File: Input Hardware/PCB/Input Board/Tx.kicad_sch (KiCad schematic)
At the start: 40 parts

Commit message: WEEEE
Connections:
- net GNDPWR is gone; now on net GND: U?.1 (PGND), U?.1 (PGND), U?.1 (PGND), U?.1 (PGND), U?.10 (PGND), U?.10 (PGND), U?.10 (PGND), U?.10 (PGND), U?.11 (PGND), U?.11 (PGND), U?.11 (PGND), U?.11 (PGND), U?.19 (LGND), U?.19 (LGND), U?.19 (LGND), U?.19 (LGND), U?.20 (PGND), U?.20 (PGND), U?.20 (PGND), U?.20 (PGND)

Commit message: input encoder and LEDs
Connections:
- net ~{SRCLR} is gone; now on net +5V: U?.8 (~{SRCLR}), U?.8 (~{SRCLR}), U?.8 (~{SRCLR}), U?.8 (~{SRCLR})

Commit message: Fix files idc
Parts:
- gave numbers to parts that had none: 40

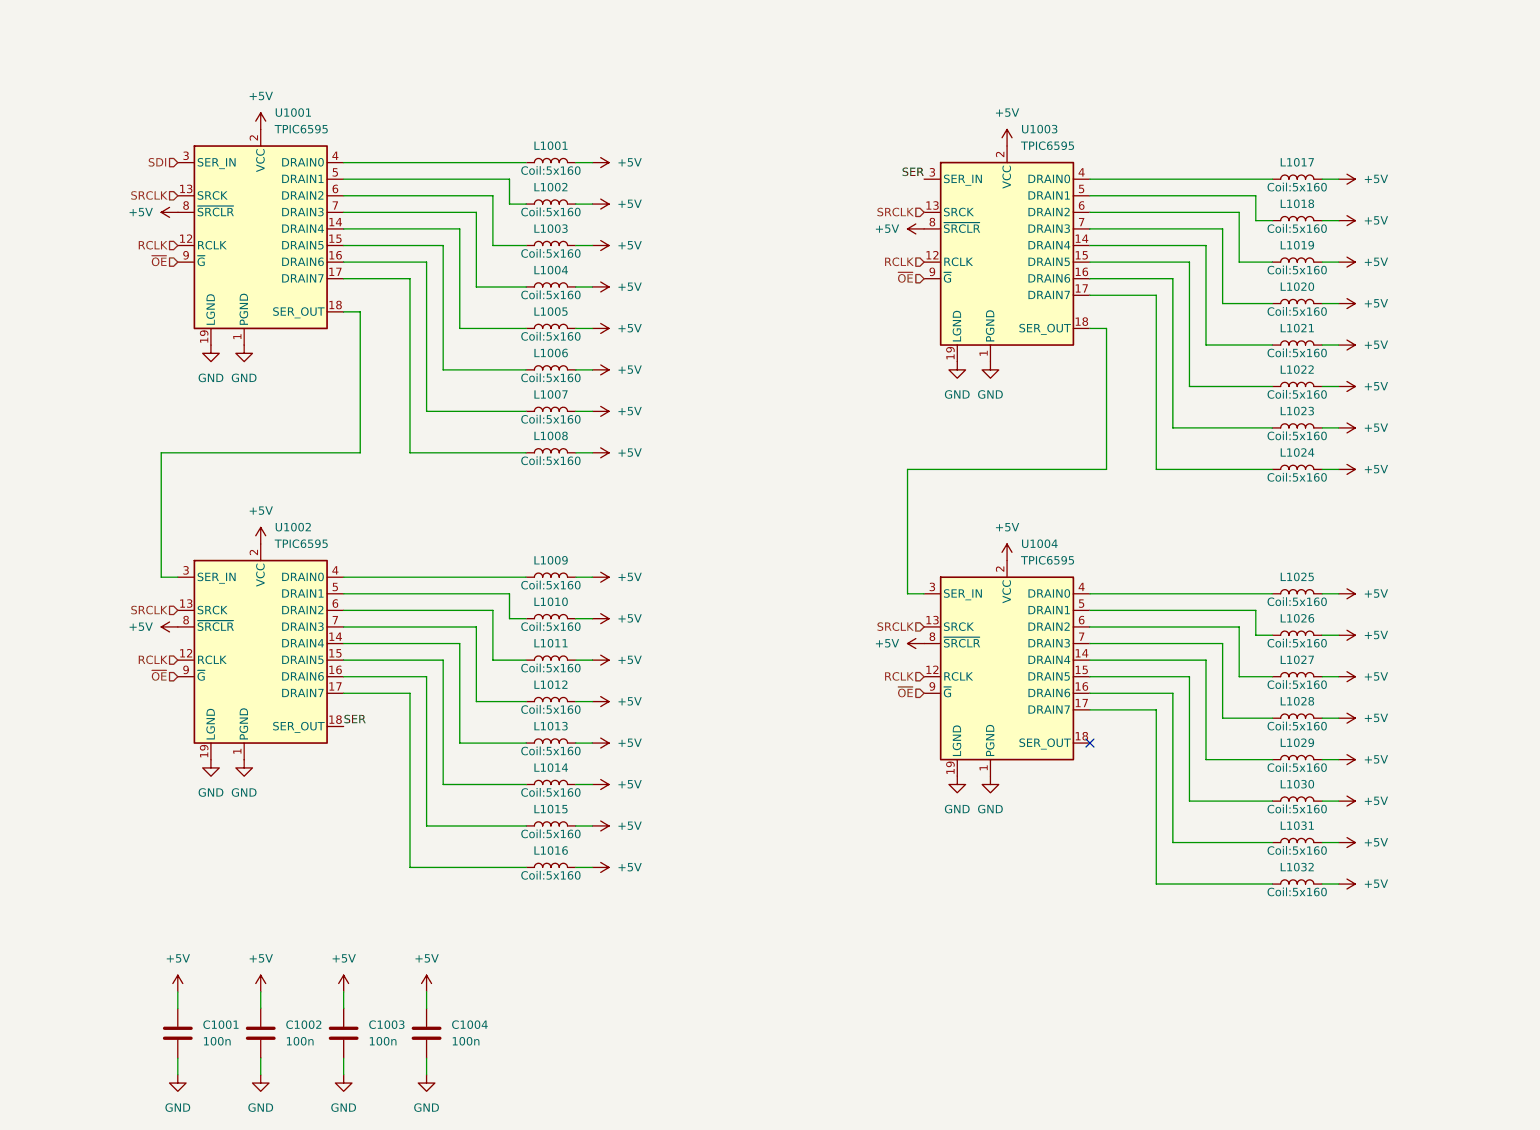
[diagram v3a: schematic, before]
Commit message: driver and root page updates
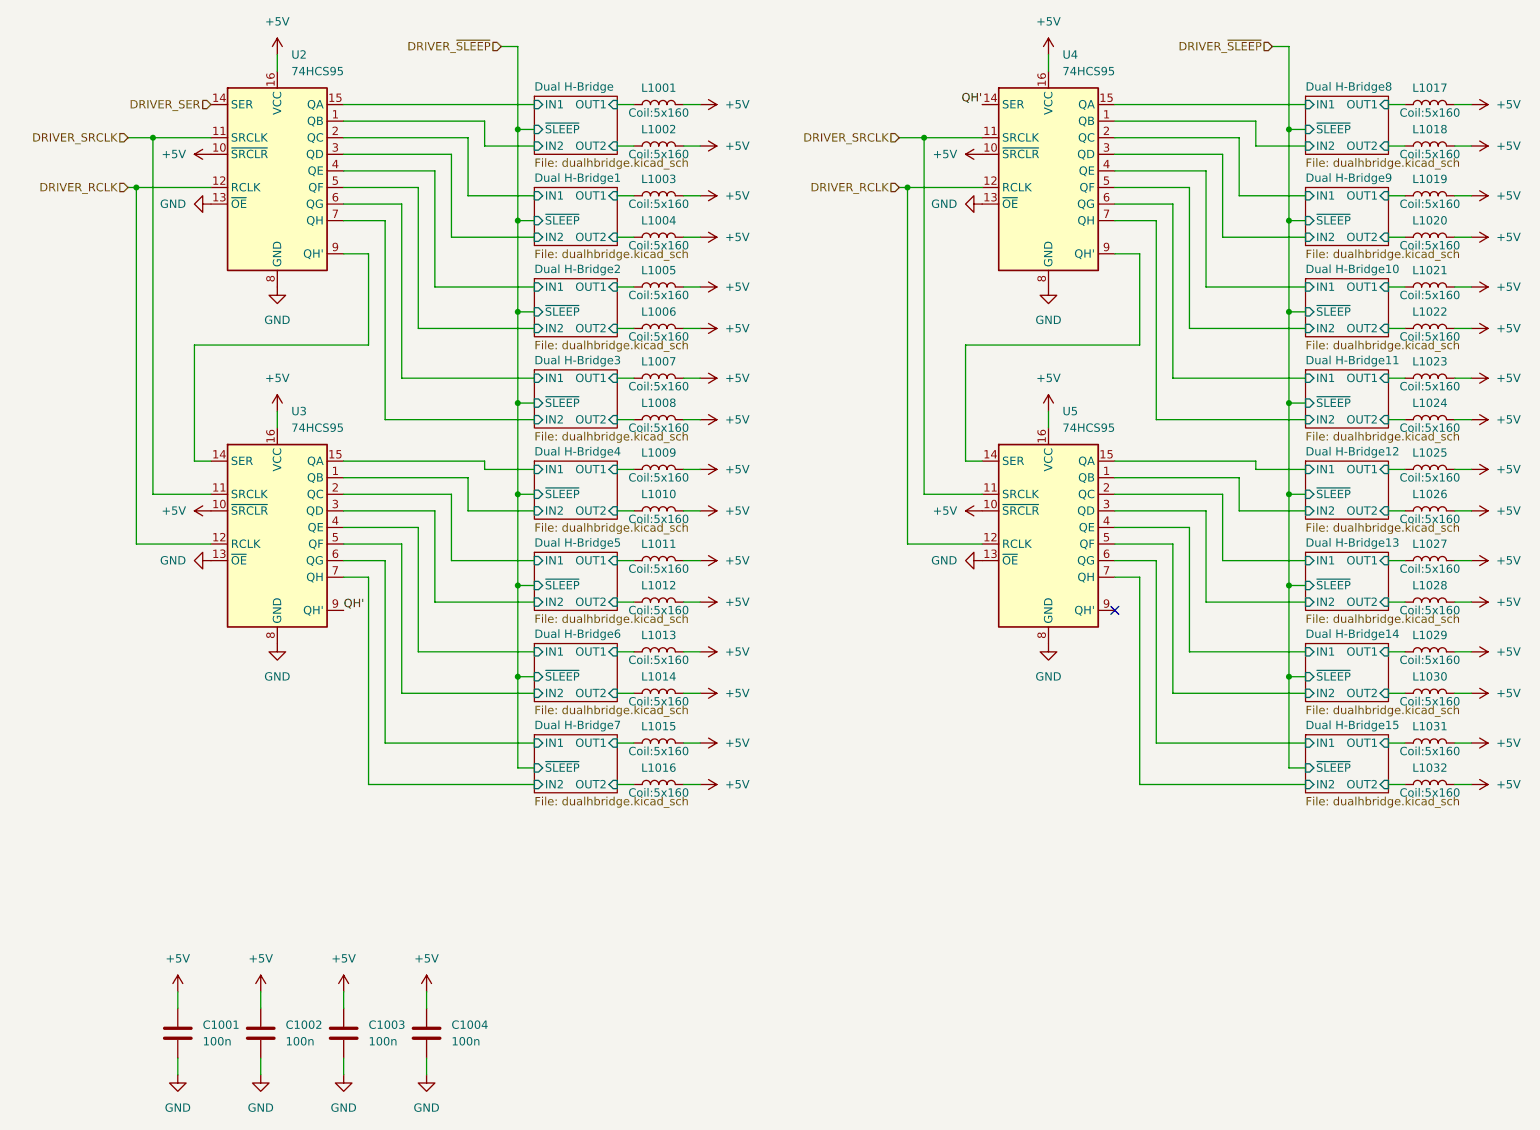
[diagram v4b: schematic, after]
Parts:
- removed U1001, U1002, U1003, U1004: TPIC6595, Package_SO:SOIC-20W_7.5x12.8mm_P1.27mm, symbol Interface_Expansion:TPIC6595
- added U2, U3, U4, U5: 74HCS95, Package_SO:SOIC-16_3.9x9.9mm_P1.27mm, symbol 74xx:74HC595
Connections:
- net +5V: now also U2.10 (~{SRCLR}), U2.16 (VCC), U3.10 (~{SRCLR}), U3.16 (VCC), U4.10 (~{SRCLR}), U4.16 (VCC), U5.10 (~{SRCLR}), U5.16 (VCC)
- net GND: now also U2.13 (~{OE}), U2.8 (GND), U3.13 (~{OE}), U3.8 (GND), U4.13 (~{OE}), U4.8 (GND), U5.13 (~{OE}), U5.8 (GND)
- net Dual H-Bridge9/OUT1: now reaches L1019.1
- net Dual H-Bridge11/OUT2: now reaches L1024.1
- net Dual H-Bridge2/OUT2: now reaches L1006.1
- net Dual H-Bridge1/OUT1: now reaches L1003.1
- net Dual H-Bridge3/OUT2: now reaches L1008.1
- net Dual H-Bridge13/OUT1: now reaches L1027.1
- net Dual H-Bridge3/OUT1: now reaches L1007.1
- net Dual H-Bridge14/OUT2: now reaches L1030.1
- net Dual H-Bridge12/OUT2: now reaches L1026.1
- net Dual H-Bridge1/OUT2: now reaches L1004.1
- net Dual H-Bridge6/OUT1: now reaches L1013.1
- net Dual H-Bridge6/OUT2: now reaches L1014.1
- net Dual H-Bridge5/OUT1: now reaches L1011.1
- net Dual H-Bridge8/OUT1: now reaches L1017.1
- net Dual H-Bridge4/OUT2: now reaches L1010.1
- net Dual H-Bridge15/OUT1: now reaches L1031.1
- net Dual H-Bridge/OUT2: now reaches L1002.1
- net Dual H-Bridge10/OUT1: now reaches L1021.1
- net Dual H-Bridge10/OUT2: now reaches L1022.1
- net Dual H-Bridge11/OUT1: now reaches L1023.1
- net Dual H-Bridge8/OUT2: now reaches L1018.1
- net Dual H-Bridge9/OUT2: now reaches L1020.1
- net Dual H-Bridge/OUT1: now reaches L1001.1
- net Dual H-Bridge2/OUT1: now reaches L1005.1
- net Dual H-Bridge7/OUT1: now reaches L1015.1
- net Dual H-Bridge7/OUT2: now reaches L1016.1
- net Dual H-Bridge4/OUT1: now reaches L1009.1
- net Dual H-Bridge5/OUT2: now reaches L1012.1
- net Dual H-Bridge14/OUT1: now reaches L1029.1
- net Dual H-Bridge15/OUT2: now reaches L1032.1
- net Dual H-Bridge12/OUT1: now reaches L1025.1
- net Dual H-Bridge13/OUT2: now reaches L1028.1
- new net: U2.9 (QH'), U3.14 (SER)
- new net: U4.9 (QH'), U5.14 (SER)
- new net DRIVER_RCLK: U2.12 (RCLK), U3.12 (RCLK), U4.12 (RCLK), U5.12 (RCLK)
- new net DRIVER_SER: U2.14 (SER)
- new net DRIVER_SRCLK: U2.11 (SRCLK), U3.11 (SRCLK), U4.11 (SRCLK), U5.11 (SRCLK)
- new net Dual H-Bridge/IN1: U2.15 (QA)
- new net Dual H-Bridge/IN2: U2.1 (QB)
- new net Dual H-Bridge1/IN1: U2.2 (QC)
- new net Dual H-Bridge1/IN2: U2.3 (QD)
- new net Dual H-Bridge10/IN1: U4.4 (QE)
- new net Dual H-Bridge10/IN2: U4.5 (QF)
- new net Dual H-Bridge11/IN1: U4.6 (QG)
- new net Dual H-Bridge11/IN2: U4.7 (QH)
- new net Dual H-Bridge12/IN1: U5.15 (QA)
- new net Dual H-Bridge12/IN2: U5.1 (QB)
- new net Dual H-Bridge13/IN1: U5.2 (QC)
- new net Dual H-Bridge13/IN2: U5.3 (QD)
- new net Dual H-Bridge14/IN1: U5.4 (QE)
- new net Dual H-Bridge14/IN2: U5.5 (QF)
- new net Dual H-Bridge15/IN1: U5.6 (QG)
- new net Dual H-Bridge15/IN2: U5.7 (QH)
- new net Dual H-Bridge2/IN1: U2.4 (QE)
- new net Dual H-Bridge2/IN2: U2.5 (QF)
- new net Dual H-Bridge3/IN1: U2.6 (QG)
- new net Dual H-Bridge3/IN2: U2.7 (QH)
- new net Dual H-Bridge4/IN1: U3.15 (QA)
- new net Dual H-Bridge4/IN2: U3.1 (QB)
- new net Dual H-Bridge5/IN1: U3.2 (QC)
- new net Dual H-Bridge5/IN2: U3.3 (QD)
- new net Dual H-Bridge6/IN1: U3.4 (QE)
- new net Dual H-Bridge6/IN2: U3.5 (QF)
- new net Dual H-Bridge7/IN1: U3.6 (QG)
- new net Dual H-Bridge7/IN2: U3.7 (QH)
- new net Dual H-Bridge8/IN1: U4.15 (QA)
- new net Dual H-Bridge8/IN2: U4.1 (QB)
- new net Dual H-Bridge9/IN1: U4.2 (QC)
- new net Dual H-Bridge9/IN2: U4.3 (QD)
- new net QH': U3.9 (QH'), U4.14 (SER)
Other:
- added sheet Dual H-Bridge (dualhbridge.kicad_sch)
- added sheet Dual H-Bridge1 (dualhbridge.kicad_sch)
- added sheet Dual H-Bridge10 (dualhbridge.kicad_sch)
- added sheet Dual H-Bridge11 (dualhbridge.kicad_sch)
- added sheet Dual H-Bridge12 (dualhbridge.kicad_sch)
- added sheet Dual H-Bridge13 (dualhbridge.kicad_sch)
- added sheet Dual H-Bridge14 (dualhbridge.kicad_sch)
- added sheet Dual H-Bridge15 (dualhbridge.kicad_sch)
- added sheet Dual H-Bridge2 (dualhbridge.kicad_sch)
- added sheet Dual H-Bridge3 (dualhbridge.kicad_sch)
- added sheet Dual H-Bridge4 (dualhbridge.kicad_sch)
- added sheet Dual H-Bridge5 (dualhbridge.kicad_sch)
- added sheet Dual H-Bridge6 (dualhbridge.kicad_sch)
- added sheet Dual H-Bridge7 (dualhbridge.kicad_sch)
- added sheet Dual H-Bridge8 (dualhbridge.kicad_sch)
- added sheet Dual H-Bridge9 (dualhbridge.kicad_sch)
- moved on the sheet: L1001, L1002, L1003, L1004, L1005, L1006, L1007, L1008, L1009, L1010, L1011, L1012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

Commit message: Revert "driver and root page updates"
This reverts commit 54e272777a4dc0dc5d2e3cf73da3d3a01278b96a.
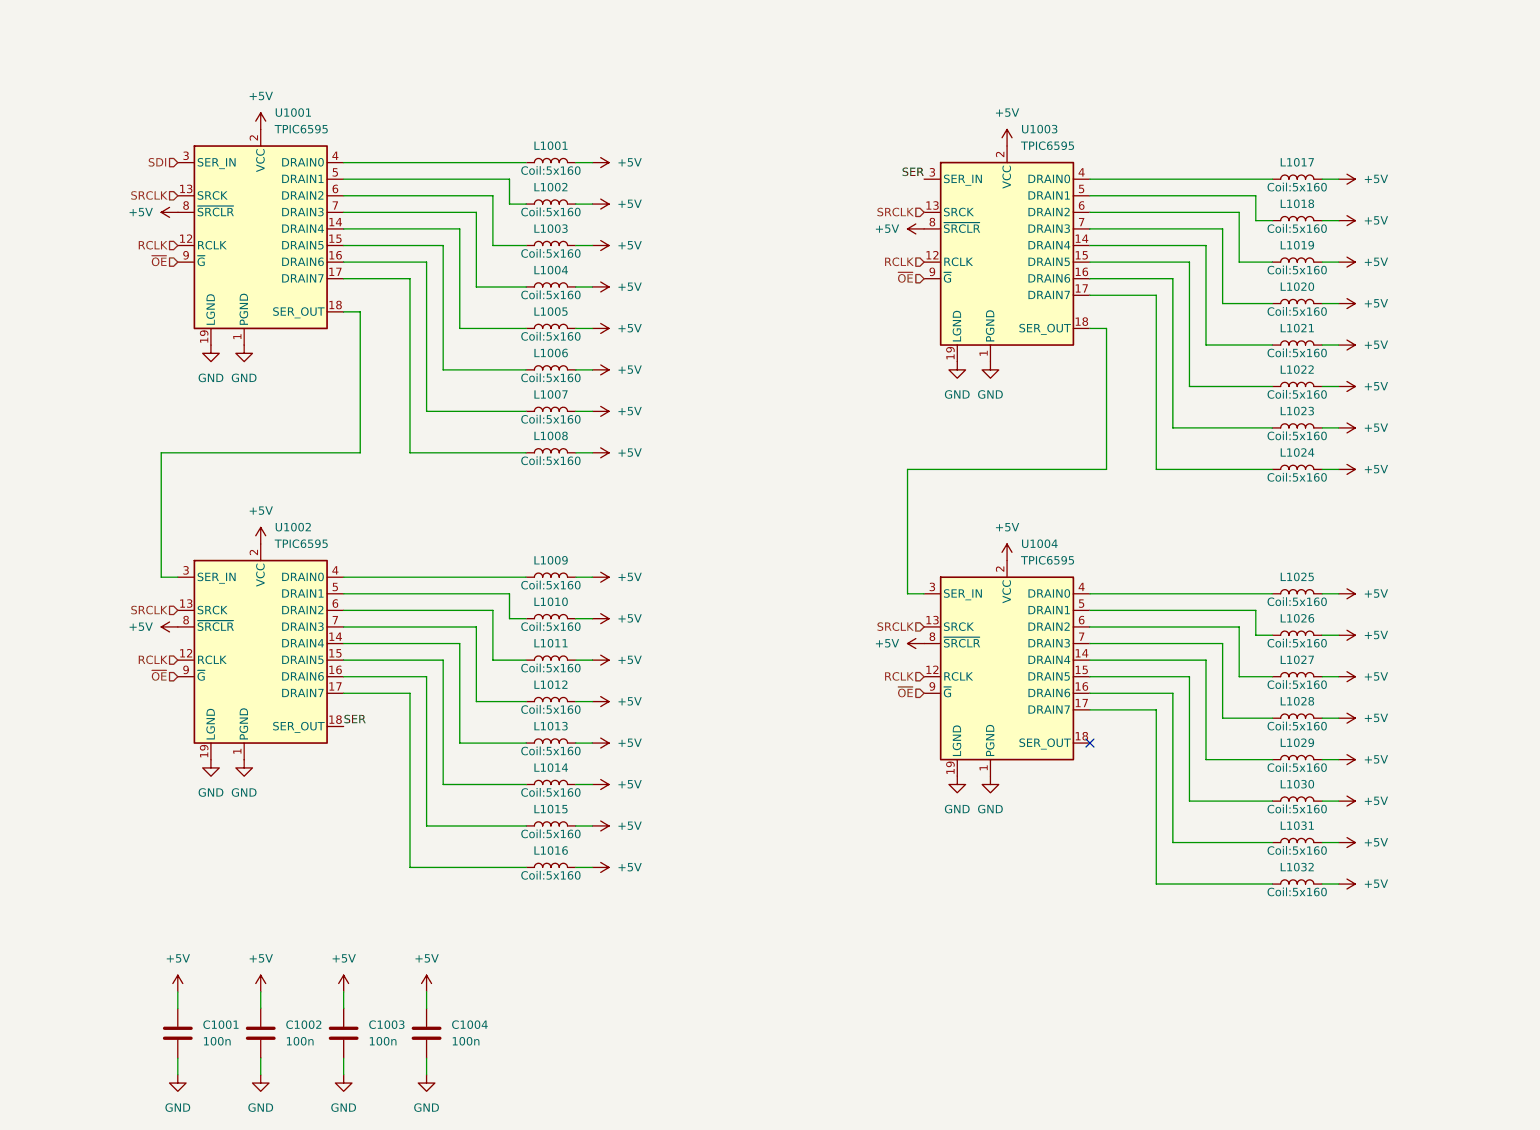
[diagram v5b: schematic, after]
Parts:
- removed U2, U3, U4, U5: 74HCS95, Package_SO:SOIC-16_3.9x9.9mm_P1.27mm, symbol 74xx:74HC595
- added U1001, U1002, U1003, U1004: TPIC6595, Package_SO:SOIC-20W_7.5x12.8mm_P1.27mm, symbol Interface_Expansion:TPIC6595
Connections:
- net +5V: now also U1001.2 (VCC), U1001.8 (~{SRCLR}), U1002.2 (VCC), U1002.8 (~{SRCLR}), U1003.2 (VCC), U1003.8 (~{SRCLR}), U1004.2 (VCC), U1004.8 (~{SRCLR})
- net GND: now also U1001.1 (PGND), U1001.10 (PGND), U1001.11 (PGND), U1001.19 (LGND), U1001.20 (PGND), U1002.1 (PGND), U1002.10 (PGND), U1002.11 (PGND), U1002.19 (LGND), U1002.20 (PGND), U1003.1 (PGND), U1003.10 (PGND), U1003.11 (PGND), U1003.19 (LGND), U1003.20 (PGND), U1004.1 (PGND), U1004.10 (PGND), U1004.11 (PGND), U1004.19 (LGND), U1004.20 (PGND)
- net Dual H-Bridge/OUT1: no longer names the net of L1001.1
- net Dual H-Bridge/OUT1: now also U1001.4 (DRAIN0)
- net Dual H-Bridge/OUT2: no longer names the net of L1002.1
- net Dual H-Bridge/OUT2: now also U1001.5 (DRAIN1)
- net Dual H-Bridge1/OUT1: no longer names the net of L1003.1
- net Dual H-Bridge1/OUT1: now also U1001.6 (DRAIN2)
- net Dual H-Bridge1/OUT2: no longer names the net of L1004.1
- net Dual H-Bridge1/OUT2: now also U1001.7 (DRAIN3)
- net Dual H-Bridge10/OUT1: no longer names the net of L1021.1
- net Dual H-Bridge10/OUT1: now also U1003.14 (DRAIN4)
- net Dual H-Bridge10/OUT2: no longer names the net of L1022.1
- net Dual H-Bridge10/OUT2: now also U1003.15 (DRAIN5)
- net Dual H-Bridge11/OUT1: no longer names the net of L1023.1
- net Dual H-Bridge11/OUT1: now also U1003.16 (DRAIN6)
- net Dual H-Bridge11/OUT2: no longer names the net of L1024.1
- net Dual H-Bridge11/OUT2: now also U1003.17 (DRAIN7)
- net Dual H-Bridge12/OUT1: no longer names the net of L1025.1
- net Dual H-Bridge12/OUT1: now also U1004.4 (DRAIN0)
- net Dual H-Bridge12/OUT2: no longer names the net of L1026.1
- net Dual H-Bridge12/OUT2: now also U1004.5 (DRAIN1)
- net Dual H-Bridge13/OUT1: no longer names the net of L1027.1
- net Dual H-Bridge13/OUT1: now also U1004.6 (DRAIN2)
- net Dual H-Bridge13/OUT2: no longer names the net of L1028.1
- net Dual H-Bridge13/OUT2: now also U1004.7 (DRAIN3)
- net Dual H-Bridge14/OUT1: no longer names the net of L1029.1
- net Dual H-Bridge14/OUT1: now also U1004.14 (DRAIN4)
- net Dual H-Bridge14/OUT2: no longer names the net of L1030.1
- net Dual H-Bridge14/OUT2: now also U1004.15 (DRAIN5)
- net Dual H-Bridge15/OUT1: no longer names the net of L1031.1
- net Dual H-Bridge15/OUT1: now also U1004.16 (DRAIN6)
- net Dual H-Bridge15/OUT2: no longer names the net of L1032.1
- net Dual H-Bridge15/OUT2: now also U1004.17 (DRAIN7)
- net Dual H-Bridge2/OUT1: no longer names the net of L1005.1
- net Dual H-Bridge2/OUT1: now also U1001.14 (DRAIN4)
- net Dual H-Bridge2/OUT2: no longer names the net of L1006.1
- net Dual H-Bridge2/OUT2: now also U1001.15 (DRAIN5)
- net Dual H-Bridge3/OUT1: no longer names the net of L1007.1
- net Dual H-Bridge3/OUT1: now also U1001.16 (DRAIN6)
- net Dual H-Bridge3/OUT2: no longer names the net of L1008.1
- net Dual H-Bridge3/OUT2: now also U1001.17 (DRAIN7)
- net Dual H-Bridge4/OUT1: no longer names the net of L1009.1
- net Dual H-Bridge4/OUT1: now also U1002.4 (DRAIN0)
- net Dual H-Bridge4/OUT2: no longer names the net of L1010.1
- net Dual H-Bridge4/OUT2: now also U1002.5 (DRAIN1)
- net Dual H-Bridge5/OUT1: no longer names the net of L1011.1
- net Dual H-Bridge5/OUT1: now also U1002.6 (DRAIN2)
- net Dual H-Bridge5/OUT2: no longer names the net of L1012.1
- net Dual H-Bridge5/OUT2: now also U1002.7 (DRAIN3)
- net Dual H-Bridge6/OUT1: no longer names the net of L1013.1
- net Dual H-Bridge6/OUT1: now also U1002.14 (DRAIN4)
- net Dual H-Bridge6/OUT2: no longer names the net of L1014.1
- net Dual H-Bridge6/OUT2: now also U1002.15 (DRAIN5)
- net Dual H-Bridge7/OUT1: no longer names the net of L1015.1
- net Dual H-Bridge7/OUT1: now also U1002.16 (DRAIN6)
- net Dual H-Bridge7/OUT2: no longer names the net of L1016.1
- net Dual H-Bridge7/OUT2: now also U1002.17 (DRAIN7)
- net Dual H-Bridge8/OUT1: no longer names the net of L1017.1
- net Dual H-Bridge8/OUT1: now also U1003.4 (DRAIN0)
- net Dual H-Bridge8/OUT2: no longer names the net of L1018.1
- net Dual H-Bridge8/OUT2: now also U1003.5 (DRAIN1)
- net Dual H-Bridge9/OUT1: no longer names the net of L1019.1
- net Dual H-Bridge9/OUT1: now also U1003.6 (DRAIN2)
- net Dual H-Bridge9/OUT2: no longer names the net of L1020.1
- net Dual H-Bridge9/OUT2: now also U1003.7 (DRAIN3)
- new net: U1003.18 (SER_OUT), U1004.3 (SER_IN)
- new net: U1001.18 (SER_OUT), U1002.3 (SER_IN)
- new net RCLK: U1001.12 (RCLK), U1002.12 (RCLK), U1003.12 (RCLK), U1004.12 (RCLK)
- new net SDI: U1001.3 (SER_IN)
- new net SER: U1002.18 (SER_OUT), U1003.3 (SER_IN)
- new net SRCLK: U1001.13 (SRCK), U1002.13 (SRCK), U1003.13 (SRCK), U1004.13 (SRCK)
- new net ~{OE}: U1001.9 (~{G}), U1002.9 (~{G}), U1003.9 (~{G}), U1004.9 (~{G})
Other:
- removed sheet Dual H-Bridge
- removed sheet Dual H-Bridge1
- removed sheet Dual H-Bridge10
- removed sheet Dual H-Bridge11
- removed sheet Dual H-Bridge12
- removed sheet Dual H-Bridge13
- removed sheet Dual H-Bridge14
- removed sheet Dual H-Bridge15
- removed sheet Dual H-Bridge2
- removed sheet Dual H-Bridge3
- removed sheet Dual H-Bridge4
- removed sheet Dual H-Bridge5
- removed sheet Dual H-Bridge6
- removed sheet Dual H-Bridge7
- removed sheet Dual H-Bridge8
- removed sheet Dual H-Bridge9
- moved on the sheet: L1001, L1002, L1003, L1004, L1005, L1006, L1007, L1008, L1009, L1010, L1011, L1012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
